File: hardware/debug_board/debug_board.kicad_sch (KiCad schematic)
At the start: 6 parts, among them CN1 Conn_05x02_Female, J11 Conn_02x05_Counter_Clockwise, J13 Conn_02x16_Counter_Clockwise, J15 Conn_02x16_Counter_Clockwise, J5 Conn_02x03_Odd_Even, J6 Conn_01x32_MountingPin

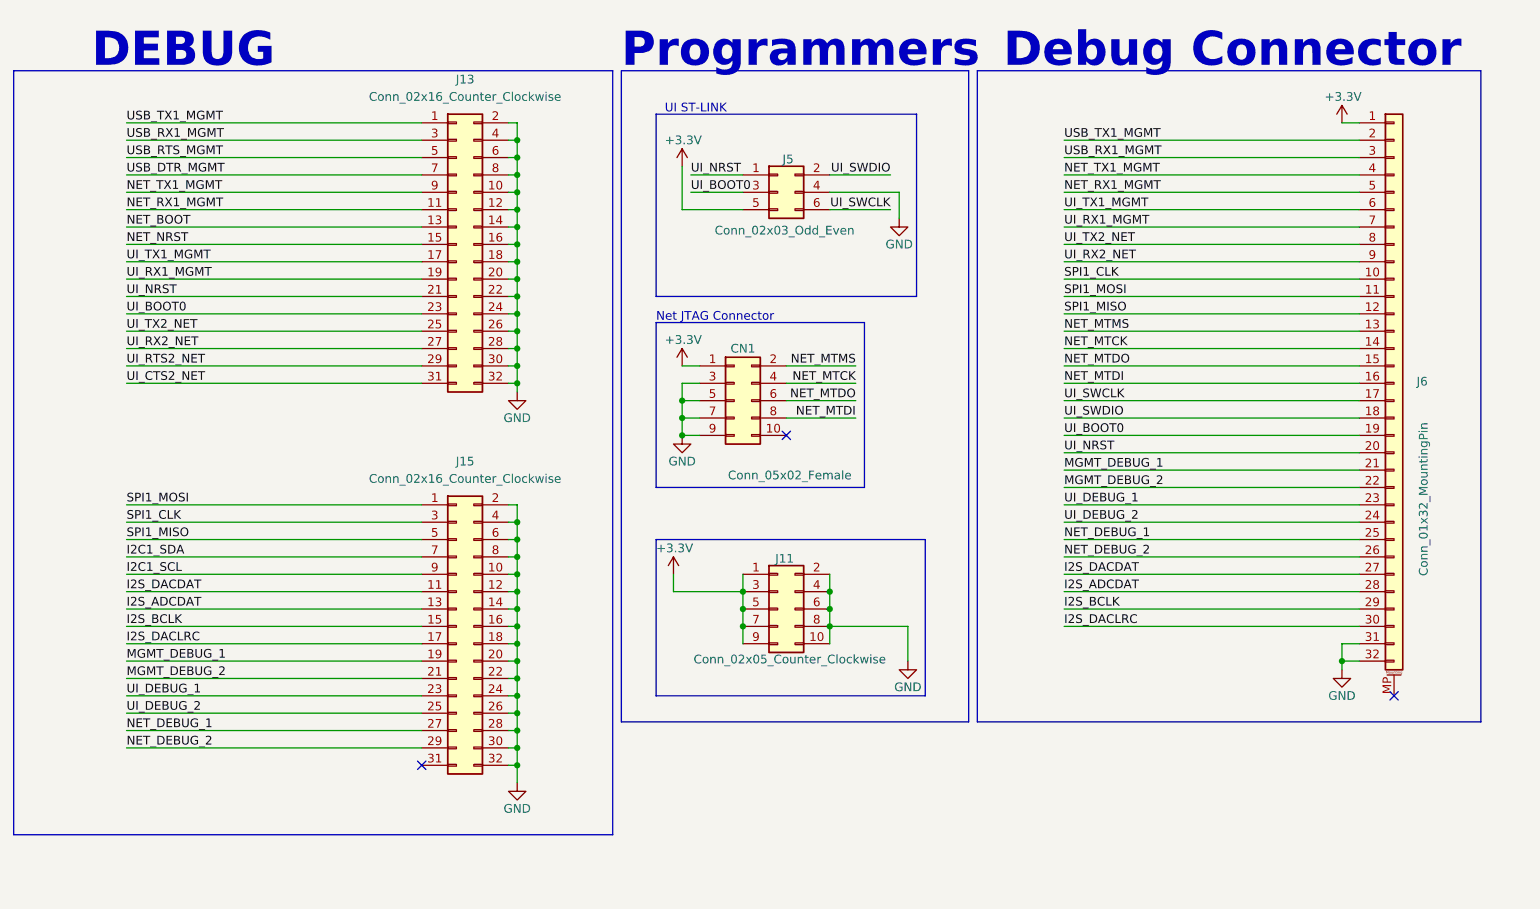
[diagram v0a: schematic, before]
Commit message: Created debug board
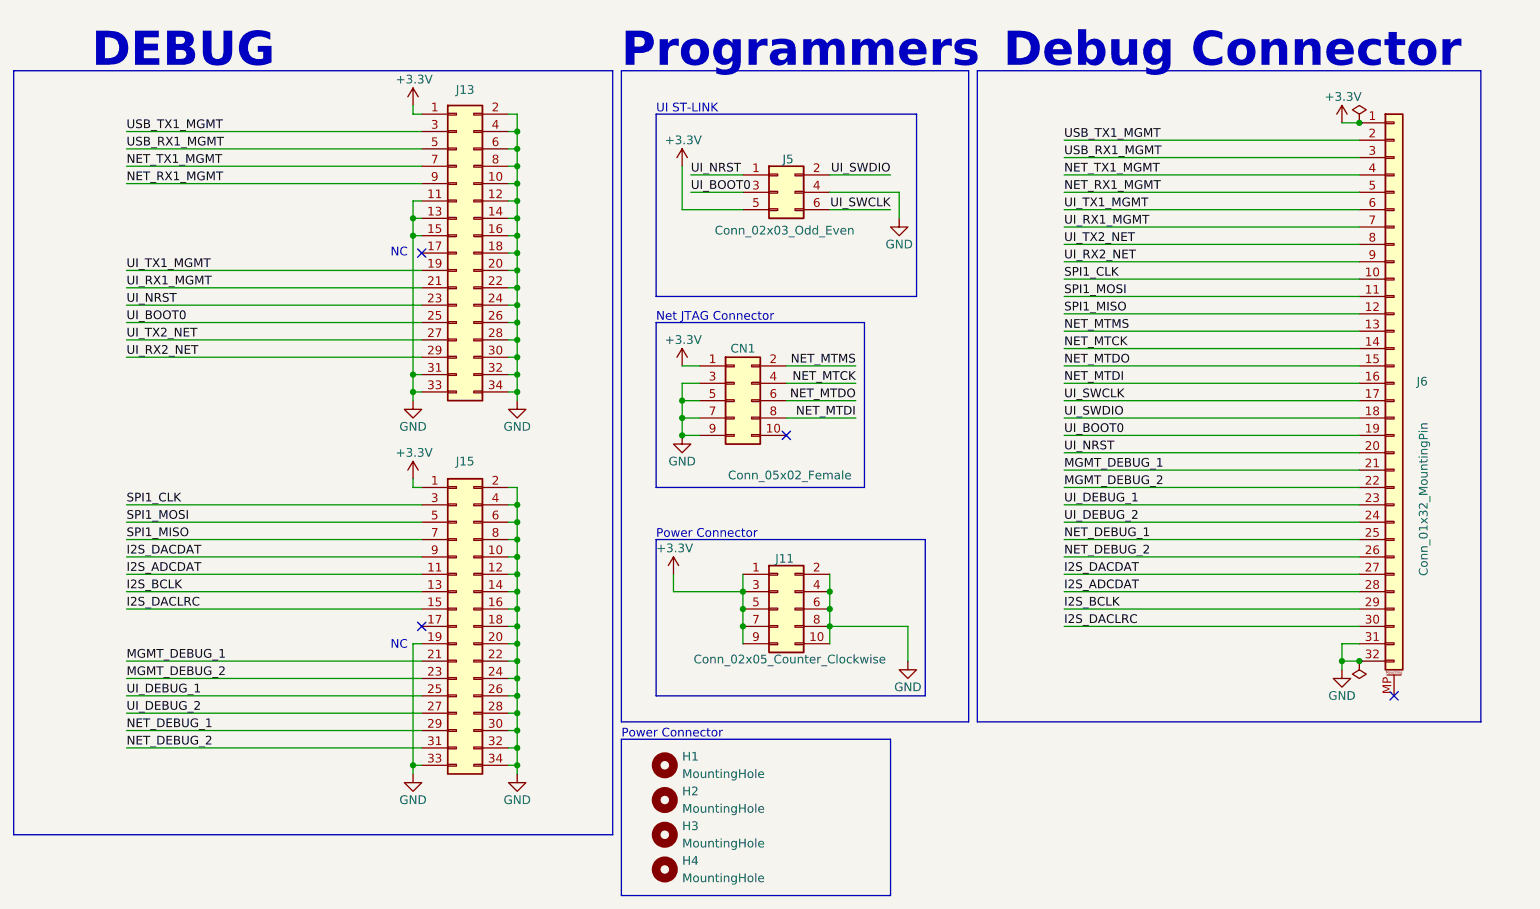
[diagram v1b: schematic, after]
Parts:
- added H1, H2, H3, H4: MountingHole, MountingHole:MountingHole_2.7mm_M2.5, symbol Mechanical:MountingHole
- J13, J15: value Conn_02x16_Counter_Clockwise -> Conn_02x17_Counter_Clockwise; footprint Connector_PinHeader_2.54mm:PinHeader_2x16_P2.54mm_Vertical_SMD -> Connector_PinHeader_2.54mm:PinHeader_2x17_P2.54mm_Vertical_SMD; symbol Connector_Generic:Conn_02x16_Odd_Even -> Connector_Generic:Conn_02x17_Odd_Even; JLCPCB Part # C3975161 -> C22436164
- J6: JLCPCB Part # (none) -> C597985
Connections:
- net I2C1_SCL is gone; now on net I2S_DACDAT: J15.9 (Pin_9)
- net I2C1_SDA is gone; now on net SPI1_MISO: J15.7 (Pin_7)
- net NET_BOOT is gone; now on net GND: J13.13 (Pin_13)
- net NET_NRST is gone; now on net GND: J13.15 (Pin_15)
- net UI_CTS2_NET is gone; now on net GND: J13.31 (Pin_31)
- net UI_RTS2_NET is gone; now on net UI_RX2_NET: J13.29 (Pin_29)
- net USB_DTR_MGMT is gone; now on net NET_TX1_MGMT: J13.7 (Pin_7)
- net USB_RTS_MGMT is gone; now on net USB_RX1_MGMT: J13.5 (Pin_5)
- net +3.3V: now also J13.1 (Pin_1), J15.1 (Pin_1)
- net GND: now also J13.11 (Pin_11), J13.33 (Pin_33), J13.34 (Pin_34), J15.19 (Pin_19), J15.33 (Pin_33), J15.34 (Pin_34)
- net I2S_ADCDAT: now also J15.11 (Pin_11); no longer J15.13 (Pin_13)
- net I2S_BCLK: now also J15.13 (Pin_13); no longer J15.15 (Pin_15)
- net I2S_DACDAT: no longer J15.11 (Pin_11)
- net I2S_DACLRC: now also J15.15 (Pin_15); no longer J15.17 (Pin_17)
- net MGMT_DEBUG_1: now also J15.21 (Pin_21); no longer J15.19 (Pin_19)
- net MGMT_DEBUG_2: now also J15.23 (Pin_23); no longer J15.21 (Pin_21)
- net NET_DEBUG_1: now also J15.29 (Pin_29); no longer J15.27 (Pin_27)
- net NET_DEBUG_2: now also J15.31 (Pin_31); no longer J15.29 (Pin_29)
- net NET_RX1_MGMT: now also J13.9 (Pin_9); no longer J13.11 (Pin_11)
- net NET_TX1_MGMT: no longer J13.9 (Pin_9)
- net SPI1_MISO: no longer J15.5 (Pin_5)
- net SPI1_MOSI: now also J15.5 (Pin_5); no longer J15.1 (Pin_1)
- net UI_BOOT0: now also J13.25 (Pin_25); no longer J13.23 (Pin_23)
- net UI_DEBUG_1: now also J15.25 (Pin_25); no longer J15.23 (Pin_23)
- net UI_DEBUG_2: now also J15.27 (Pin_27); no longer J15.25 (Pin_25)
- net UI_NRST: now also J13.23 (Pin_23); no longer J13.21 (Pin_21)
- net UI_RX1_MGMT: now also J13.21 (Pin_21); no longer J13.19 (Pin_19)
- net UI_RX2_NET: no longer J13.27 (Pin_27)
- net UI_TX1_MGMT: now also J13.19 (Pin_19); no longer J13.17 (Pin_17)
- net UI_TX2_NET: now also J13.27 (Pin_27); no longer J13.25 (Pin_25)
- net USB_RX1_MGMT: no longer J13.3 (Pin_3)
- net USB_TX1_MGMT: now also J13.3 (Pin_3); no longer J13.1 (Pin_1)
- no-connect marks 3 -> 4
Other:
- note added: "NC"
- note added: "Power Connector"

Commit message: Updated schematic and pcb to output a file jlcpcb expects
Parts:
- J11, J13, J15: FT Rotation Offset (none) -> 90
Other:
- title: HACTAR SCHEMATIC - Finn Berg & Brett Regnier -> Hactar Debug Schematic - Brett Regnier
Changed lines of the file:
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@@
 	(paper "A4")
 	(title_block
-		(title "HACTAR SCHEMATIC - Finn Berg & Brett Regnier")
-		(date "2026-06-08")
-		(rev "EV19")
+		(title "Hactar Debug Schematic - Brett Regnier")
+		(date "2026-07-27")
+		(rev "EV1")
 		(company "CISCO SYSTEMS INC")
 	)
@@
 		(in_bom no)
 		(on_board yes)
-		(in_pos_files yes)
+		(in_pos_files no)
 		(dnp no)
 		(fields_autoplaced yes)
@@
 			)
 		)
+		(property "FT Rotation Offset" "90"
+			(at 135.89 106.68 0)
+			(hide yes)
+			(show_name no)
+			(do_not_autoplace no)
+			(effects
+				(font
+					(size 1.27 1.27)
+				)
+			)
+		)
 		(pin "6"
 		)
@@
 		(in_bom no)
 		(on_board yes)
-		(in_pos_files yes)
+		(in_pos_files no)
 		(dnp no)
 		(fields_autoplaced yes)
@@
 			)
 		)
+		(property "FT Rotation Offset" "90"
+			(at 88.9 109.22 0)
+			(hide yes)
+			(show_name no)
+			(do_not_autoplace no)
+			(effects
+				(font
+					(size 1.27 1.27)
+				)
+			)
+		)
 		(pin "20"
 		)
@@
 		(in_bom no)
 		(on_board yes)
-		(in_pos_files yes)
+		(in_pos_files no)
 		(dnp no)
 		(fields_autoplaced yes)
@@
 		(in_bom no)
 		(on_board yes)
-		(in_pos_files yes)
+		(in_pos_files no)
 		(dnp no)
 		(fields_autoplaced yes)
@@
 			(at 88.9 54.61 0)
 			(hide yes)
+			(show_name no)
+			(do_not_autoplace no)
+			(effects
+				(font
+					(size 1.27 1.27)
+				)
+			)
+		)
+		(property "FT Rotation Offset" "90"
+			(at 88.9 54.61 0)
+			(hide yes)
